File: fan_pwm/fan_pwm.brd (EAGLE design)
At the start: 17.9 x 46.8 mm, 17 parts, among them J1 PJ-058A, U1 LTC6992CS6-4TRMPBF, U2 SN74LVC1G34DBVR, U3 MIC5205-5.0YM5-TR

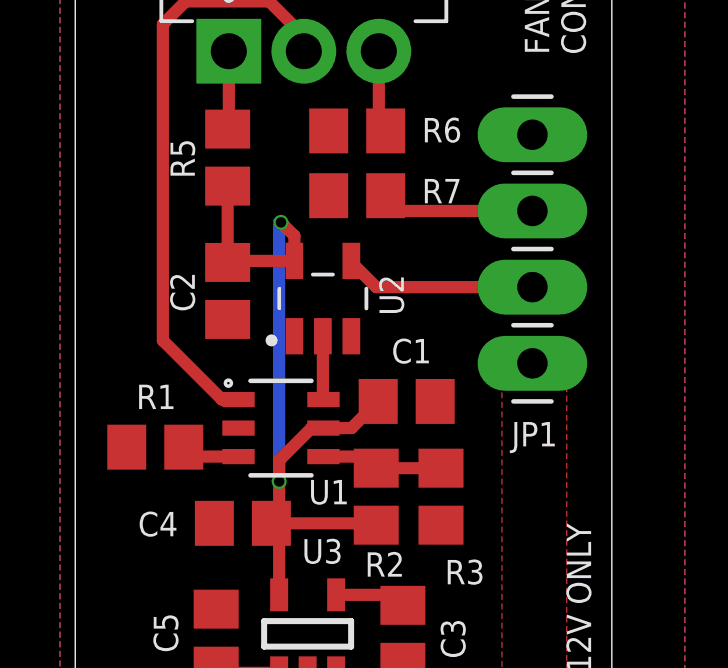
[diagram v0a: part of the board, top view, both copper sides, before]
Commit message: tacho pullup
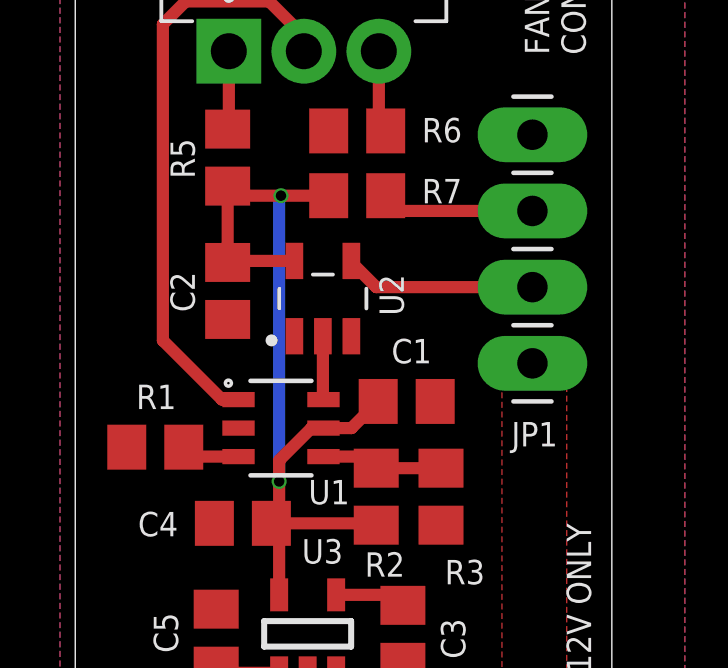
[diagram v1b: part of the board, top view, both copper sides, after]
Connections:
- net +5V: now also R7.1
- net GND: no longer R7.1
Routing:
- net +5V: track 27.3 -> 30.1 mm
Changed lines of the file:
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@@
 </element>
 <element name="R7" library="rcl" library_urn="urn:adsk.eagle:library:334" package="R0805" package3d_urn="urn:adsk.eagle:package:23553/2" value="100k" x="9.398" y="29.21" smashed="yes">
-<attribute name="NAME" x="11.557" y="28.956" size="0.8128" layer="25" ratio="16"/>
+<attribute name="NAME" x="11.557" y="28.956" size="0.8128" layer="25" font="vector" ratio="16"/>
 <attribute name="POPULARITY" value="85" x="32.258" y="-10.16" size="1.778" layer="27" display="off"/>
 <attribute name="SPICEPREFIX" value="R" x="32.258" y="-10.16" size="1.778" layer="27" display="off"/>
@@
 <contactref element="C1" pad="2"/>
 <contactref element="JP1" pad="4"/>
-<contactref element="R7" pad="1"/>
 <contactref element="R4" pad="S1"/>
 <contactref element="R4" pad="S2"/>
@@
 <wire x1="5.08" y1="26.985" x2="5.131" y2="27.036" width="0.4064" layer="1"/>
 <wire x1="5.131" y1="27.036" x2="7.305" y2="27.036" width="0.4064" layer="1"/>
-<wire x1="5.08" y1="29.53" x2="5.08" y2="26.985" width="0.4064" layer="1"/>
+<wire x1="5.08" y1="29.53" x2="5.08" y2="29.337" width="0.4064" layer="1"/>
+<wire x1="5.08" y1="29.337" x2="5.08" y2="26.985" width="0.4064" layer="1"/>
 <wire x1="8.27405" y1="21.463" x2="7.874" y2="21.463" width="0.4064" layer="1"/>
 <wire x1="7.874" y1="21.463" x2="6.797" y2="20.386" width="0.4064" layer="1"/>
 <wire x1="6.797" y1="20.386" x2="6.797" y2="19.685" width="0.4064" layer="1"/>
 <via x="6.797" y="19.685" extent="1-16" drill="0.35"/>
-<wire x1="6.797" y1="19.685" x2="6.797" y2="28.321" width="0.4064" layer="16"/>
-<wire x1="6.797" y1="28.321" x2="6.858" y2="28.321" width="0.4064" layer="16"/>
-<via x="6.858" y="28.321" extent="1-16" drill="0.35"/>
-<wire x1="6.858" y1="28.321" x2="7.305" y2="27.874" width="0.4064" layer="1"/>
-<wire x1="7.305" y1="27.874" x2="7.305" y2="27.036" width="0.4064" layer="1"/>
+<wire x1="6.797" y1="19.685" x2="6.797" y2="29.21" width="0.4064" layer="16"/>
+<wire x1="6.797" y1="29.21" x2="6.858" y2="29.21" width="0.4064" layer="16"/>
+<via x="6.858" y="29.21" extent="1-16" drill="0.35"/>
 <wire x1="6.797" y1="19.685" x2="6.797" y2="18.547" width="0.4064" layer="1"/>
 <wire x1="6.797" y1="18.547" x2="6.538" y2="18.288" width="0.4064" layer="1"/>
@@
 <wire x1="6.538" y1="18.288" x2="9.972" y2="18.288" width="0.4064" layer="1"/>
 <wire x1="9.972" y1="18.288" x2="10.033" y2="18.227" width="0.4064" layer="1"/>
+<contactref element="R7" pad="1"/>
+<wire x1="6.858" y1="29.21" x2="5.207" y2="29.21" width="0.4064" layer="1"/>
+<wire x1="5.207" y1="29.21" x2="5.08" y2="29.337" width="0.4064" layer="1"/>
+<wire x1="6.858" y1="29.21" x2="8.448" y2="29.21" width="0.4064" layer="1"/>
 </signal>
 <signal name="PWM">
